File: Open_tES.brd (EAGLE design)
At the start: 91 x 63 mm, 61 parts, among them IC2 MAX232ECWES, IC4 LP2950CZ-5.0, IC5 OPA277U, IC6 LF444CM, IC7 PIC16F1937P, J1 RJ11-2X, U1 MIC2288YD5-TR, U2 74LVC1G10W6-7, X1 22-23-2041, X2 057-016-1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

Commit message: Changing of C_FILT value 22->10uc to simplify the circuit. The same capacitor is already used on the board : C2-MIC5270
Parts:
- C_FILT: value 22µF -> 10µF
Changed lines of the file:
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@@
 </element>
 <element name="C2Q" library="rcl" package="C0805" value="22pF" x="28.2575" y="30.7975" rot="MR270">
-<attribute name="OC_FARNELL" value="1856180RL" x="28.2575" y="30.7975" size="1.778" layer="28" rot="MR270" display="off"/>
+<attribute name="OC_FARNELL" value="1856180" x="28.2575" y="30.7975" size="1.778" layer="28" rot="MR270" display="off"/>
 </element>
 <element name="R_MCLR" library="rcl" package="0204/7" value="10k" x="64.77" y="36.195">
@@
 </element>
 <element name="R5" library="rcl" package="M0805" value="17K8" x="12.3825" y="46.355" rot="R180">
-<attribute name="OC_FARNELL" value="1811059" x="12.3825" y="46.355" size="1.778" layer="27" rot="R180" display="off"/>
+<attribute name="OC_FARNELL" value="1575931" x="12.3825" y="46.355" size="1.778" layer="27" rot="R180" display="off"/>
 </element>
 <element name="R_BUZZ" library="rcl" package="R0805" value="2K7" x="53.34" y="17.78" rot="MR90">
@@
 <attribute name="MPN" value="" x="17.4625" y="11.43" size="1.778" layer="28" rot="MR0" display="off"/>
 <attribute name="MF" value="" x="17.4625" y="11.43" size="1.778" layer="28" rot="MR0" display="off"/>
-<attribute name="OC_FARNELL" value="8395934" x="17.4625" y="11.43" size="1.778" layer="28" rot="MR0" display="off"/>
+<attribute name="OC_FARNELL" value="1554029" x="17.4625" y="11.43" size="1.778" layer="28" rot="MR0" display="off"/>
 </element>
 <element name="R11" library="rcl" package="0204/7" value="620" x="6.985" y="33.02" rot="R270">
@@
 </element>
 <element name="C1Q" library="rcl" package="C0805" value="22pF" x="25.0825" y="30.7975" rot="MR90">
-<attribute name="OC_FARNELL" value="1856180RL" x="25.0825" y="30.7975" size="1.778" layer="28" rot="MR90" display="off"/>
+<attribute name="OC_FARNELL" value="1856180" x="25.0825" y="30.7975" size="1.778" layer="28" rot="MR90" display="off"/>
 </element>
 <element name="POWER" library="con-molex" package="6410-02" value="22-27-2021-02" x="64.135" y="42.545">
@@
 <attribute name="MF" value="" x="64.135" y="42.545" size="1.778" layer="27" display="off"/>
 <attribute name="OC_FARNELL" value="143126+1654528+1462641" x="64.135" y="42.545" size="1.778" layer="27" display="off"/>
-<attribute name="FARNELL" value="143126+1654528+1462641" x="64.135" y="42.545" size="1.778" layer="27" display="off"/>
 </element>
 <element name="IC4" library="v-reg" package="TO92" value="LP2950CZ-5.0" x="68.2625" y="55.88" rot="R180">
@@
 </element>
 <element name="C2_MIC" library="rcl" package="C0805" value="4.7µF" x="56.8325" y="50.4825" rot="MR180">
-<attribute name="OC_FARNELL" value="2458302" x="56.8325" y="50.4825" size="1.778" layer="28" rot="MR180" display="off"/>
+<attribute name="OC_FARNELL" value="2426962" x="56.8325" y="50.4825" size="1.778" layer="28" rot="MR180" display="off"/>
 </element>
 <element name="IC2" library="maxim-6b" package="SO16" value="MAX232ECWES" x="66.9925" y="13.335" rot="MR270">
@@
 </element>
 <element name="C3_PUSH" library="rcl" package="C0805" value="0.01µF" x="33.02" y="13.97" rot="MR0">
-<attribute name="OC_FARNELL" value="1414662RL" x="33.02" y="13.97" size="1.778" layer="28" rot="MR0" display="off"/>
+<attribute name="OC_FARNELL" value="1414662" x="33.02" y="13.97" size="1.778" layer="28" rot="MR0" display="off"/>
 </element>
 <element name="C2_PUSH" library="rcl" package="C0805" value="0.01µF" x="33.02" y="11.43" rot="MR0">
-<attribute name="OC_FARNELL" value="1414662RL" x="33.02" y="11.43" size="1.778" layer="28" rot="MR0" display="off"/>
+<attribute name="OC_FARNELL" value="1414662" x="33.02" y="11.43" size="1.778" layer="28" rot="MR0" display="off"/>
 </element>
 <element name="C1_PUSH" library="rcl" package="C0805" value="0.01µF" x="33.02" y="8.89" rot="MR0">
-<attribute name="OC_FARNELL" value="1414662RL" x="33.02" y="8.89" size="1.778" layer="28" rot="MR0" display="off"/>
+<attribute name="OC_FARNELL" value="1414662" x="33.02" y="8.89" size="1.778" layer="28" rot="MR0" display="off"/>
 </element>
-<element name="C_FILT" library="rcl" package="C0805" value="22µF" x="37.1475" y="33.02" rot="MR0">
-<attribute name="OC_FARNELL" value="499365" x="37.1475" y="33.02" size="1.778" layer="28" rot="MR0" display="off"/>
+<element name="C_FILT" library="rcl" package="C0805" value="10µF" x="37.1475" y="33.02" rot="MR0">
+<attribute name="OC_FARNELL" value="2346934" x="37.1475" y="33.02" size="1.778" layer="28" rot="MR0" display="off"/>
 </element>
 <element name="R_FILT" library="rcl" package="R0805" value="10K" x="37.1475" y="35.56" rot="MR0">
-<attribute name="OC_FARNELL" value="2129113" x="37.1475" y="35.56" size="1.778" layer="28" rot="MR0" display="off"/>
+<attribute name="OC_FARNELL" value="9332383" x="37.1475" y="35.56" size="1.778" layer="28" rot="MR0" display="off"/>
 </element>
 <element name="CD_LCD" library="rcl" package="C0805" value="0.1µF" x="9.8425" y="15.24" rot="MR0">
@@
 </element>
 <element name="R1_MIC" library="rcl" package="R0805" value="28.7KR" x="56.8325" y="56.8325" rot="MR0">
-<attribute name="OC_FARNELL" value="2303698" x="56.8325" y="56.8325" size="1.778" layer="28" rot="MR0" display="off"/>
+<attribute name="OC_FARNELL" value="1167459" x="56.8325" y="56.8325" size="1.778" layer="28" rot="MR0" display="off"/>
 </element>
 <element name="R2_MIC" library="rcl" package="R0805" value="1.24KR" x="56.8325" y="54.2925" rot="MR180">

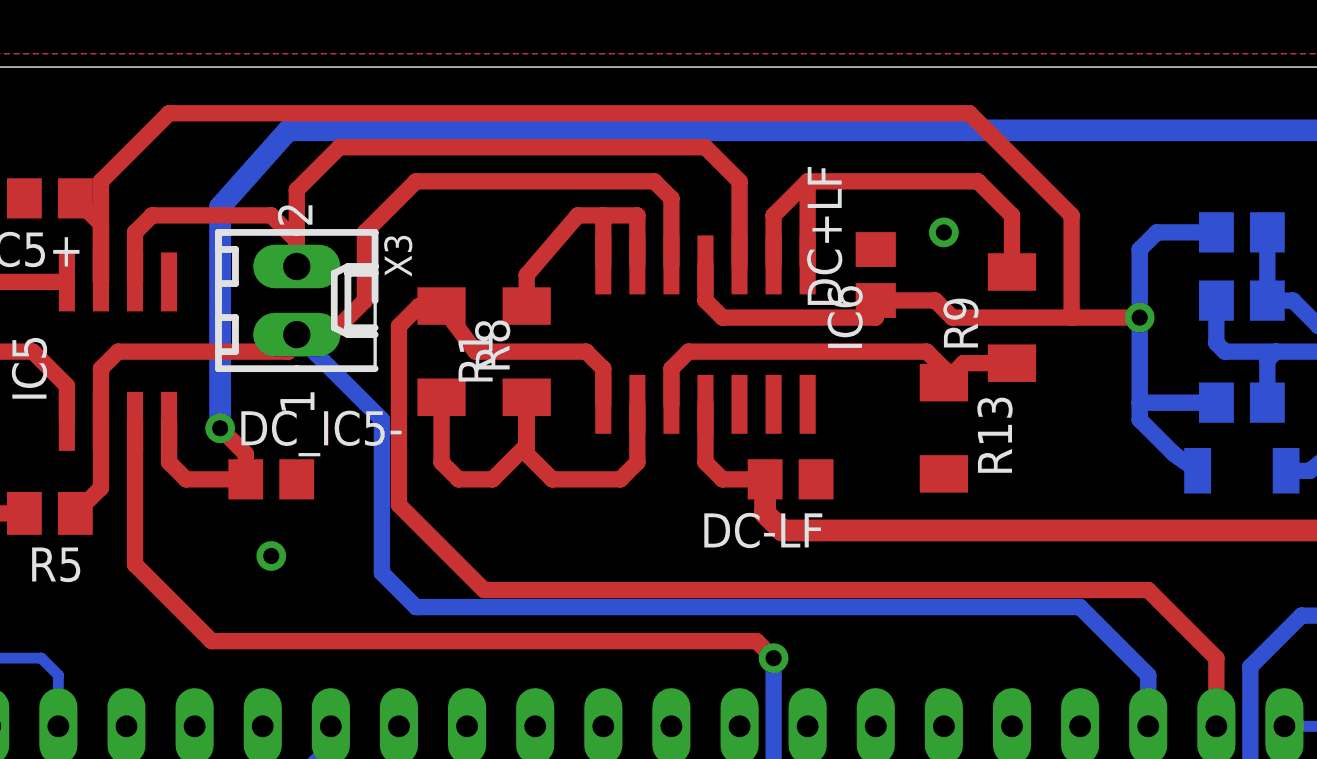
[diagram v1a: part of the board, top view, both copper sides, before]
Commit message: replace package of R1 R8 R9 R13 MELF->0805 to reduce the cost. Update version 2.0->2.1 in files
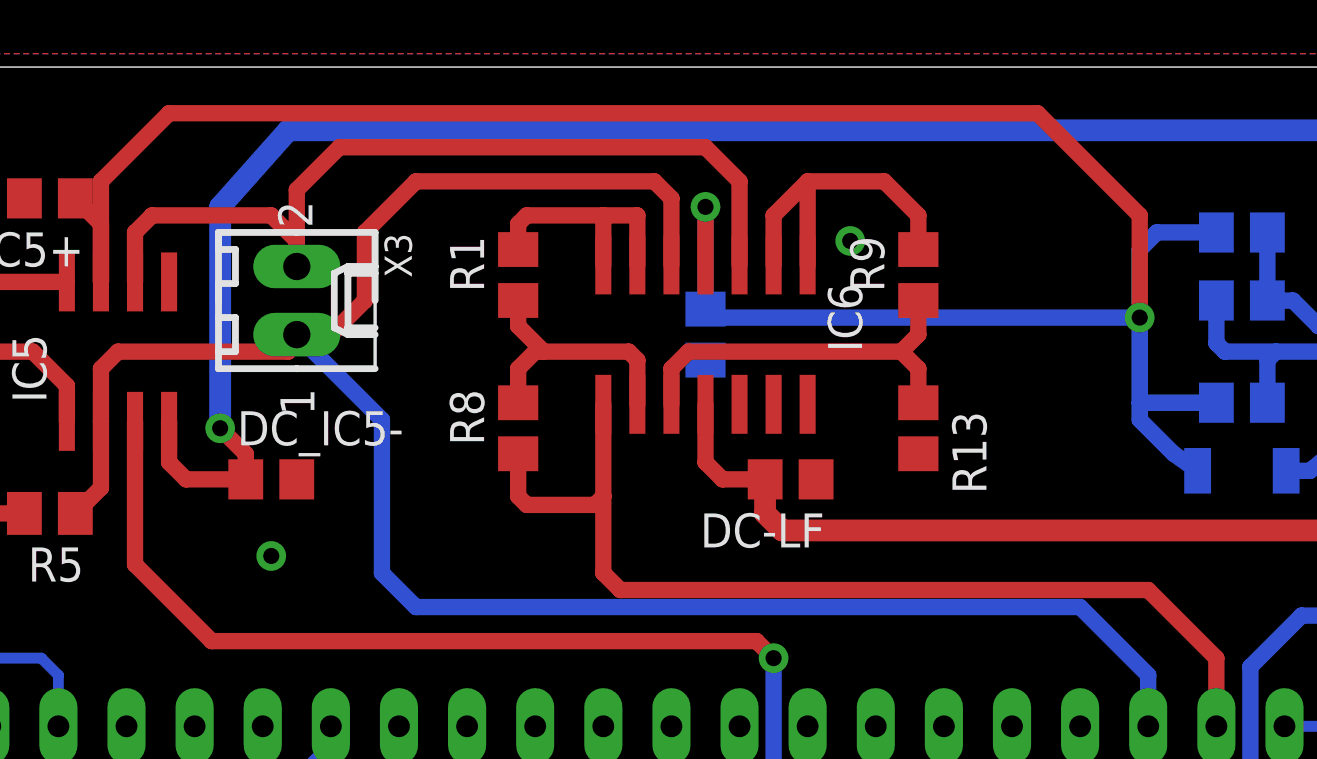
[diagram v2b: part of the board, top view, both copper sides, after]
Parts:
- R1, R13, R8, R9: device rcl:M1406 -> rcl:R0805
- moved DC+LF 6.73 mm to (36.8, 53.0), flipped to the bottom, turned to 270 degrees
- moved R8 4.04 mm to (29.8, 49.5), turned to 90 degrees
- moved R9 3.84 mm to (44.8, 55.2)
- moved R1 2.88 mm to (29.8, 55.2)
- moved R13 0.95 mm to (44.8, 49.5)
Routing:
- net UCAPT: track 52.4 -> 38.0 mm
- net N$14: track 17.2 -> 10.1 mm
- net +30V: track 83.8 -> 89.6 mm, vias 1 -> 2
- net N$17: track 17.0 -> 12.7 mm
- net N$13: track 15.4 -> 14.5 mm
- net N$2: track 10.00 -> 9.22 mm

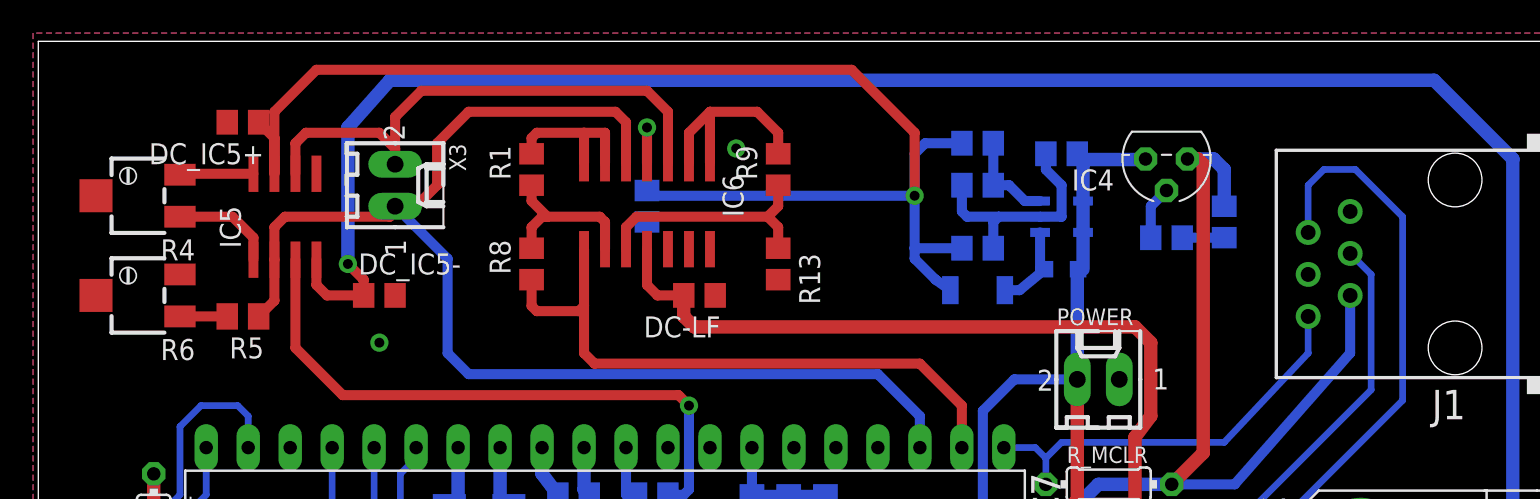
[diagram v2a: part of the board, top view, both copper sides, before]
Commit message: Fixing of several mistakes concerning component references. Changing of package for the trimmers R4 R6.
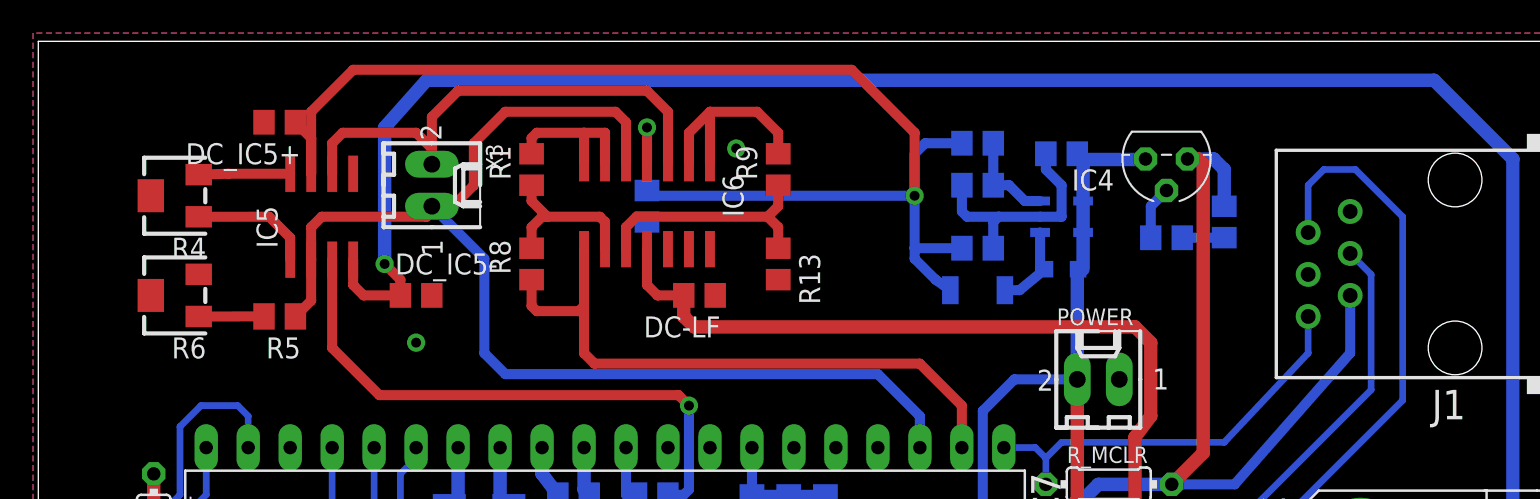
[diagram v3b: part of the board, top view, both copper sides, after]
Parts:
- R4, R6: device rcl:RTRIM3224X -> rcl:RTRIM3214W
- moved R4 2.22 mm to (8.26, 53.7)
- moved R6 2.22 mm to (8.26, 47.6)
- moved DC_IC5+ 2.22 mm to (14.6, 58.1)
- moved DC_IC5- 2.22 mm to (22.9, 47.6)
- moved IC5 2.22 mm to (17.1, 52.4)
- moved R5 2.22 mm to (14.6, 46.4)
- moved X3 2.22 mm to (23.8, 54.3)
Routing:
- net ICAPT: track 76.6 -> 72.2 mm
- net +30V: track 89.6 -> 87.4 mm
- net N$29: track 33.2 -> 30.9 mm
- net N$19: track 39.6 -> 37.4 mm
- net -5V: track 236.3 -> 234.1 mm
- net N$4: track 2.86 -> 3.95 mm
- net N$28: track 6.30 -> 7.39 mm
- net N$16: track 4.45 -> 5.54 mm
